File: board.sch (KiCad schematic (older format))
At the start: 25 parts, among them J1 Z-AXIS, J10 Conn_01x02_Male, J11 Conn_01x04_Male, J12 CHOOSE, J2 Y-AXIS, J3 Y-AXIS, J4 X-AXIS, J5 12-36V, J6 12V, J7 Conn_02x14_Odd_Even, J8 12-36V, J9 CNC_OUT2, K1 SANYOU_SRD_Form_C

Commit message: Add more details (extra components, footprints and 3d models)
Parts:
- added C5, C6: 100n, Capacitor_SMD:C_1206_3216Metric, symbol Device:C
- added C7, C8, C9: 100n, Capacitor_SMD:C_0805_2012Metric, symbol Device:C
- added D1, D2, D4: LED, LED_SMD:LED_0603_1608Metric, symbol Device:LED
- added D3: SS54, Diode_SMD:D_2512_6332Metric, symbol pspice:DIODE
- added D5: LED, Diode_SMD:D_MiniMELF, symbol Device:LED
- added L1: 470, Inductor_SMD:L_Vishay_IHLP-4040, symbol Device:L
- added Q1: Y2, Package_TO_SOT_SMD:SC-59, symbol Device:Q_NPN_BCE
- added Q2: WJ0625A, Package_TO_SOT_SMD:TO-252-3_TabPin2, symbol Developower:WJ0625A
- added R1: 10K, Resistor_SMD:R_0805_2012Metric, symbol Device:R
- added R2: 1k8, Resistor_SMD:R_0805_2012Metric, symbol Device:R
- added R3: 2k, Resistor_SMD:R_0805_2012Metric, symbol Device:R
- added R4: 16k, Resistor_SMD:R_0805_2012Metric, symbol Device:R
- added R5: 10k, Resistor_SMD:R_0805_2012Metric, symbol Device:R
- added R6: 100k, Resistor_SMD:R_0805_2012Metric, symbol Device:R
- added R7: 1k, Resistor_SMD:R_0805_2012Metric, symbol Device:R
- added R8: 4k7, Resistor_SMD:R_0805_2012Metric, symbol Device:R
- added R9: 5k, Resistor_SMD:R_0805_2012Metric, symbol Device:R
- added T1: Logo_Open_Hardware_Small, Developower:chinese-text, symbol Graphic:Logo_Open_Hardware_Small
- added U1: PC817, Package_DIP:SMDIP-4_W9.53mm, symbol Isolator:PC817
- added U2: XL4015E1, Package_TO_SOT_SMD:TO-263-5_TabPin6, symbol Developower:XL4015E1
- C1, C2, C3: value 220/25V -> 220/35V; footprint (none) -> Capacitor_SMD:CP_Elec_8x10
- C4: footprint (none) -> Capacitor_SMD:CP_Elec_10x10.5
- J1: value Z-AXIS -> Z; footprint Connector_PinHeader_2.54mm:PinHeader_1x04_P2.54mm_Vertical -> Connector_JST:JST_PH_S4B-PH-K_1x04_P2.00mm_Horizontal
- J11: footprint Connector_PinHeader_2.54mm:PinHeader_1x04_P2.54mm_Vertical -> Connector_JST:JST_PH_S4B-PH-K_1x04_P2.00mm_Horizontal
- J12: renamed from J10; footprint Connector_PinHeader_2.54mm:PinHeader_1x02_P2.54mm_Vertical -> Connector_JST:JST_PH_S2B-PH-K_1x02_P2.00mm_Horizontal
- J13: renamed from J3; value Y-AXIS -> Y; footprint Connector_PinHeader_2.54mm:PinHeader_1x04_P2.54mm_Vertical -> Connector_JST:JST_PH_S4B-PH-K_1x04_P2.00mm_Horizontal
- J14: renamed from J4; value X-AXIS -> X; footprint Connector_PinHeader_2.54mm:PinHeader_1x04_P2.54mm_Vertical -> Connector_JST:JST_PH_S4B-PH-K_1x04_P2.00mm_Horizontal
- J15: renamed from J6; footprint Connector_PinHeader_2.54mm:PinHeader_1x02_P2.54mm_Vertical -> Connector_JST:JST_PH_S2B-PH-K_1x02_P2.00mm_Horizontal
- J16: renamed from J9; footprint Connector_BarrelJack:BarrelJack_Horizontal -> Developower:BarrelJack_Horizontal
- J2: renamed from A2; footprint Module:Pololu_Breakout-16_15.2x20.3mm -> Developower:Pololu_Breakout-16_15.2x20.3mm
- J3: renamed from J2; value Y-AXIS -> Y; footprint Connector_PinHeader_2.54mm:PinHeader_1x04_P2.54mm_Vertical -> Connector_JST:JST_PH_S4B-PH-K_1x04_P2.00mm_Horizontal
- J4: renamed from A3; footprint Module:Pololu_Breakout-16_15.2x20.3mm -> Developower:Pololu_Breakout-16_15.2x20.3mm
- J5: footprint Connector_PinHeader_2.54mm:PinHeader_1x02_P2.54mm_Vertical -> Connector_JST:JST_PH_S2B-PH-K_1x02_P2.00mm_Horizontal
- J6: renamed from A4; footprint Module:Pololu_Breakout-16_15.2x20.3mm -> Developower:Pololu_Breakout-16_15.2x20.3mm
- J7: renamed from J8; footprint Connector_BarrelJack:BarrelJack_Horizontal -> Developower:BarrelJack_Horizontal
- J8: renamed from A1; footprint Module:Arduino_Nano -> Developower:Arduino_Nano
- renumbered J12 to J10, J7 to J9
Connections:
- wire segments 38 -> 40
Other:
- moved on the sheet: C1, C2, C3, C4, J1, J13, J14, J3

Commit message: Add some interconnections. Fix some missing 3d models.
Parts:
- D5: symbol Device:LED -> Device:D
- J10: value CHOOSE -> CNC/Laser
- J11: value Conn_01x04_Male -> Conn_01x03_Male; footprint Connector_JST:JST_PH_S4B-PH-K_1x04_P2.00mm_Horizontal -> Connector_JST:JST_PH_S3B-PH-K_1x03_P2.00mm_Horizontal; symbol Connector:Conn_01x04_Male -> Connector:Conn_01x03_Male
- J12: value Conn_01x02_Male -> 12V
- J15: value 12V -> 12V-36V
- J16, J7: symbol Connector:Jack-DC -> Connector:Barrel_Jack_Switch_Pin3Ring
- J8: value Arduino_Nano_v3.x -> Arduino_Nano
- J9: value Conn_02x14_Odd_Even -> Misc
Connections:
- net labels added: D10, D11, D12, D13, D2, D3, D4, D5, D6, D7, D8, D9, EN, VMOT, X.1A, X.1B, X.2A, X.2B, Y.1A, Y.1B, Y.2A, Y.2B, Z.1A, Z.1B, Z.2A, Z.2B, relay.common, relay.nc, relay.no, relay.p2, relay.p5
- net labels removed: G, P13, X+, X-, XEND_A, XEND_B, Y+, Y-, YEND_A, YEND_B, Z+, Z-, ZEND_A, ZEND_B
- wire segments 40 -> 190
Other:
- moved on the sheet: C1, C2, C3, C4, C5, C6, C7, C8, C9, D1, D2, D4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

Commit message: Connect extra signals, 90% done
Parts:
- C7, C8: symbol Device:C -> Device:C_Small
- D5: value LED -> MELF
- J10: value CNC/Laser -> Mode
- R2, R4: symbol Device:R -> Device:R_Small
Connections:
- net labels added: +12V, CNC, LASER, LASER_12V, XXXX
- net labels removed: relay.common, relay.p2
- wire segments 190 -> 234
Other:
- moved on the sheet: C1, C2, C3, C4, C5, C6, C7, C8, C9, D1, D2, D4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

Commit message: Improve connections
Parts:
- C1, C2, C3, C4: symbol Device:C -> Device:CP_Small
- D3: symbol pspice:DIODE -> Device:D_Schottky
- J11: value Conn_01x03_Male -> V_LASER
- J5: value 12-36V -> LASER
- L1: value 470 -> 47u/5A
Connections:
- net labels added: 12V_36V, SPINDLE, V_LASER, V_SPINDLE, V_STEP_MOT
- net labels removed: CNC, EN, LASER_12V, X.1A, X.1B, X.2A, X.2B, XXXX, Y.1A, Y.1B, Y.2A, Y.2B, Z.1A, Z.1B, Z.2A, Z.2B, relay.nc, relay.no
- wire segments 234 -> 271
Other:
- note added: "12-36V Input"
- note added: "CNC Circuitry"
- note added: "Laser Circuitry"
- note added: "Main Controler"
- note added: "Step Motor Controlers"
- note added: "Vout = 1.25 * (1 + R1/R2)"
- moved on the sheet: C5, C6, C7, C8, C9, D1, D2, D4, D5, J1, J10, J11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

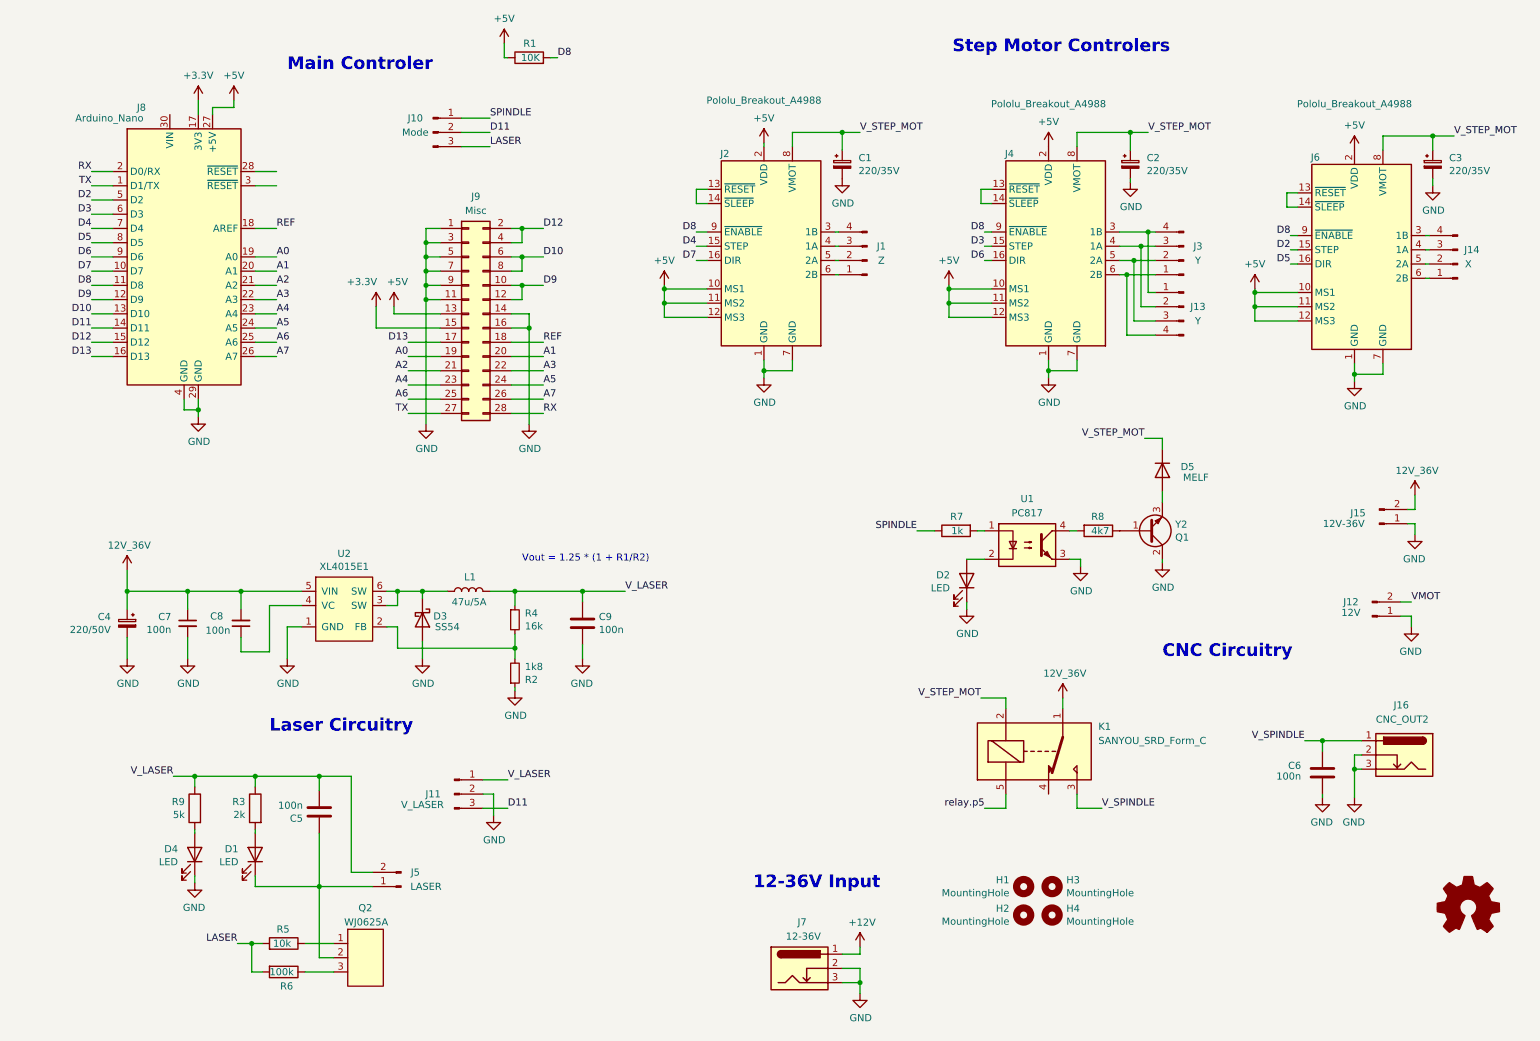
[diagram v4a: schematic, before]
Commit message: Update some parts
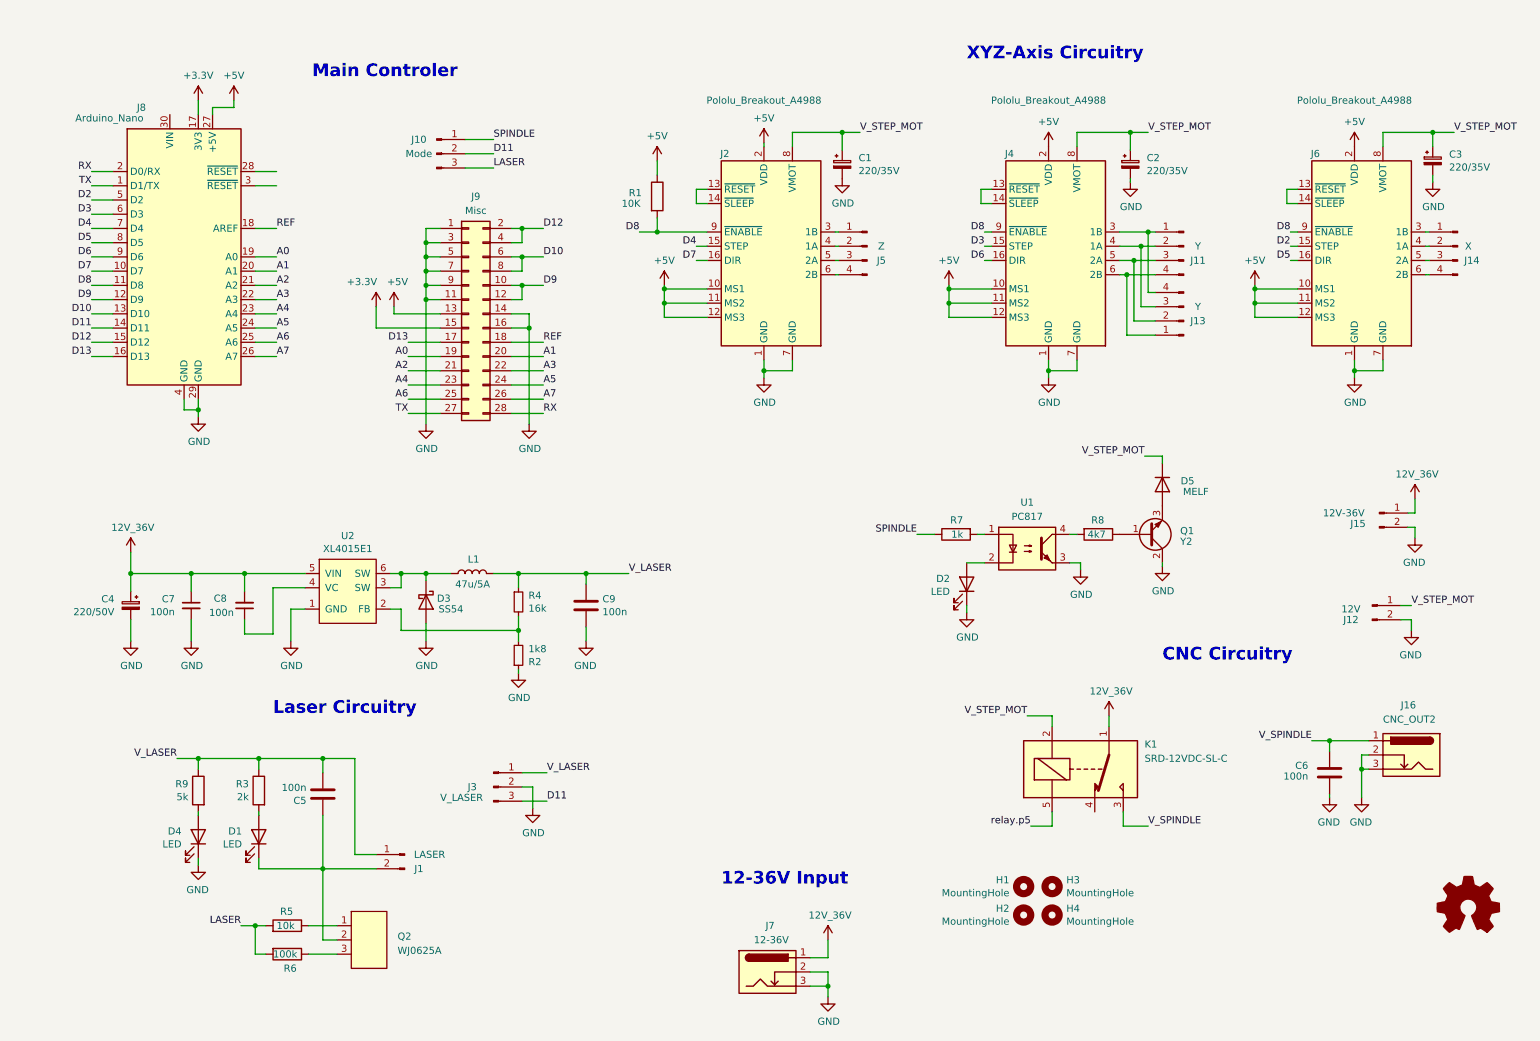
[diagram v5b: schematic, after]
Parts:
- J1: renamed from J5; footprint Connector_JST:JST_PH_S2B-PH-K_1x02_P2.00mm_Horizontal -> Developower:JST_S2B-XH-A(LF)(SN)
- J11: renamed from J3; footprint Connector_JST:JST_PH_S4B-PH-K_1x04_P2.00mm_Horizontal -> Developower:JST_S4B-XH-A(LF)(SN)
- J12, J15: footprint Connector_JST:JST_PH_S2B-PH-K_1x02_P2.00mm_Horizontal -> Developower:JST_S2B-XH-A(LF)(SN)
- J13, J14: footprint Connector_JST:JST_PH_S4B-PH-K_1x04_P2.00mm_Horizontal -> Developower:JST_S4B-XH-A(LF)(SN)
- J3: renamed from J11; footprint Connector_JST:JST_PH_S3B-PH-K_1x03_P2.00mm_Horizontal -> Developower:JST_S3B-XH-A(LF)(SN)
- J5: renamed from J1; footprint Connector_JST:JST_PH_S4B-PH-K_1x04_P2.00mm_Horizontal -> Developower:JST_S4B-XH-A(LF)(SN)
- K1: value SANYOU_SRD_Form_C -> SRD-12VDC-SL-C; footprint Relay_THT:Relay_SPDT_SANYOU_SRD_Series_Form_C -> Developower:Relay_SPDT_SANYOU_SRD_Series_Form_C
- L1: footprint Inductor_SMD:L_Vishay_IHLP-4040 -> Developower:L_Vishay_IHLP-4040
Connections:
- net +12V is gone; now on net 12V_36V: J7.1
- net VMOT is gone; now on net GND: J12.2 (Pin_2)
- net 12V_36V: now also J15.1 (Pin_1); no longer J15.2 (Pin_2)
- net GND: now also J15.2 (Pin_2); no longer J12.1 (Pin_1), J15.1 (Pin_1)
- net V_LASER: now also J1.1 (Pin_1); no longer J1.2 (Pin_2)
- net V_STEP_MOT: now also J12.1 (Pin_1)
- net at C5.1, D1.1 (K), Q2.2: now also J1.2 (Pin_2); no longer J1.1 (Pin_1)
- net at J2.3 (1B): now also J5.1 (Pin_1); no longer J5.4 (Pin_4)
- net at J2.4 (1A): now also J5.2 (Pin_2); no longer J5.3 (Pin_3)
- net at J2.5 (2A): now also J5.3 (Pin_3); no longer J5.2 (Pin_2)
- net at J2.6 (2B): now also J5.4 (Pin_4); no longer J5.1 (Pin_1)
- net at J11.4 (Pin_4), J13.1 (Pin_1): now also J4.6 (2B); no longer J4.3 (1B)
- net at J11.3 (Pin_3), J13.2 (Pin_2): now also J4.5 (2A); no longer J4.4 (1A)
- net at J11.2 (Pin_2), J13.3 (Pin_3): now also J4.4 (1A); no longer J4.5 (2A)
- net at J11.1 (Pin_1), J13.4 (Pin_4): now also J4.3 (1B); no longer J4.6 (2B)
- net at J6.3 (1B): now also J14.1 (Pin_1); no longer J14.4 (Pin_4)
- net at J6.4 (1A): now also J14.2 (Pin_2); no longer J14.3 (Pin_3)
- net at J6.5 (2A): now also J14.3 (Pin_3); no longer J14.2 (Pin_2)
- net at J6.6 (2B): now also J14.4 (Pin_4); no longer J14.1 (Pin_1)
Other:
- note added: "XYZ-Axis Circuitry"
- note removed: "Step Motor Controlers"
- note removed: "Vout = 1.25 * (1 + R1/R2)"
- moved on the sheet: C3, C4, C5, C6, C7, C8, C9, D1, D2, D3, D4, D5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

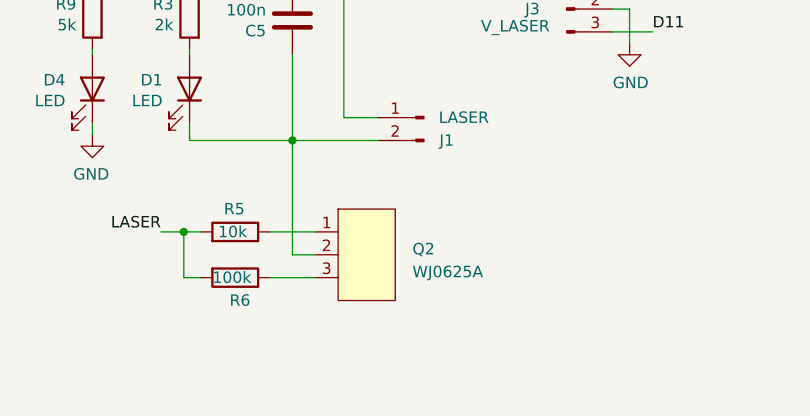
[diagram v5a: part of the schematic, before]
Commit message: Add missing connection to the GND
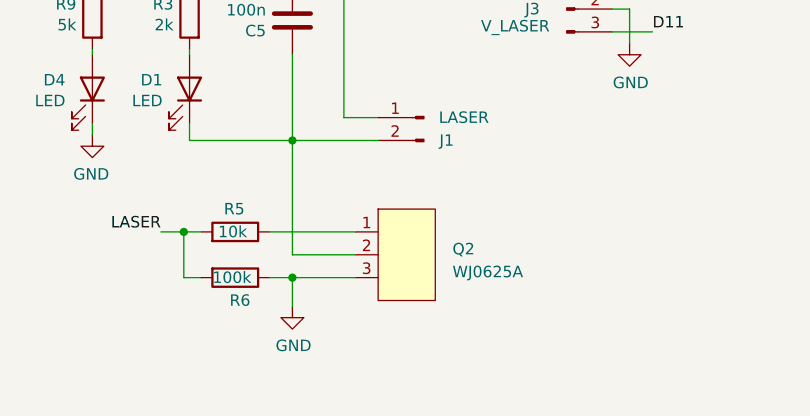
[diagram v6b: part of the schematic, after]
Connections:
- net GND: now also Q2.3, R6.1
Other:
- moved on the sheet: Q2
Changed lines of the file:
@@
 L Developower:WJ0625A Q2
 U 1 1 608700DB
-P 3025 6850
-F 0 "Q2" H 3300 6625 50  0000 L CNN
-F 1 "WJ0625A" H 3300 6525 50  0000 L CNN
-F 2 "Package_TO_SOT_SMD:TO-252-3_TabPin2" H 3025 6850 50  0001 C CNN
-F 3 "" H 3025 6850 50  0001 C CNN
-	1    3025 6850
+P 3200 6850
+F 0 "Q2" H 3475 6625 50  0000 L CNN
+F 1 "WJ0625A" H 3475 6525 50  0000 L CNN
+F 2 "Package_TO_SOT_SMD:TO-252-3_TabPin2" H 3200 6850 50  0001 C CNN
+F 3 "" H 3200 6850 50  0001 C CNN
+	1    3200 6850
 	1    0    0    -1
 $EndComp
@@
 	2300 7000 2375 7000
 Wire Wire Line
-	2675 7000 2875 7000
-Wire Wire Line
-	2675 7200 2875 7200
+	2675 7000 3050 7000
+Wire Wire Line
+	2675 7200 2775 7200
 Wire Wire Line
 	2300 7000 2200 7000
@@
 	6950 4250 7075 4250
 Wire Wire Line
-	2875 7100 2775 7100
+	3050 7100 2775 7100
 Wire Wire Line
 	8300 5525 8300 5600
@@
 Wire Wire Line
 	6325 7100 6325 7225
+Wire Wire Line
+	2775 7200 2775 7325
+Connection ~ 2775 7200
+Wire Wire Line
+	2775 7200 3050 7200
+$Comp
+L power:GND #PWR?
+U 1 1 60878EFA
+P 2775 7325
+F 0 "#PWR?" H 2775 7075 50  0001 C CNN
+F 1 "GND" H 2780 7152 50  0000 C CNN
+F 2 "" H 2775 7325 50  0001 C CNN
+F 3 "" H 2775 7325 50  0001 C CNN
+	1    2775 7325
+	1    0    0    -1
+$EndComp
 $EndSCHEMATC
